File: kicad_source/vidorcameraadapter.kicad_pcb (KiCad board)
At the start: 2 copper layers, 62 x 47 mm, 44 parts, among them CN1 CONN_02X26, CN2 CONN_02X10, CN3 CONN_01X03

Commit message: added RGB led
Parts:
- removed W13, W14, W6, W7, W8: TEST_1P, wire_pads:SolderWirePad_single_1mmSMD
- added R19: 10k, resistors:R_0603, F.Cu at (147.3, 111.8)
- added R20: 10k, resistors:R_0603, F.Cu at (147.3, 114.5)
- added R21: 10k, resistors:R_0603, F.Cu at (151.0, 111.8)
- added R22: 10k, resistors:R_0603, F.Cu at (147.3, 117.1)
- added R23: 0R, resistors:R_0603, F.Cu at (90.0, 121.0)
- added R24: 0R, resistors:R_0603, F.Cu at (92.0, 121.0)
- added R25: 1k, resistors:R_0603, F.Cu at (156.0, 133.0)
- added R26: 1k, resistors:R_0603, F.Cu at (163.0, 126.0)
- added R27: 1k, resistors:R_0603, F.Cu at (171.0, 118.0)
- added R28: 1k, resistors:R_0603, F.Cu at (165.2, 131.0)
- added R29: 1k, resistors:R_0603, F.Cu at (169.0, 124.0)
- added R30: 1k, resistors:R_0603, F.Cu at (176.8, 118.0)
- added R31: 1k, resistors:R_0603, F.Cu at (172.0, 131.0)
- added R32: 1k, resistors:R_0603, F.Cu at (175.0, 125.0)
- R1, R10, R11, R12, R13, R14, R15, R16, R17, R18, R2, R3, R4, R5, R6, R7, R8, R9: value R_0603 -> 33R
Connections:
- CN1 pad 13: /RSVD9 -> /LED_R
- CN1 pad 14: /RSVD10 -> /SDA_V
- CN1 pad 16: /RSVD11 -> /SCL_V
- CN1 pad 17: /RSVD12 -> /LED_G
- CN1 pad 19: /RSVD13 -> /LED_B
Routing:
- net /SDA: track 3.49 -> 47.7 mm
- net /SCL: track 2.85 -> 47.0 mm
- net /SCL_V: track 0.00 -> 5.60 mm
- net /SDA_V: track 0.00 -> 5.06 mm
- net /RSVD11: track 3.63 -> 0.00 mm
- net /RSVD10: track 3.46 -> 0.00 mm
- net /RSVD9: track 2.33 -> 0.00 mm
- net /LED_R: track 0.00 -> 2.33 mm
- net /RSVD13: track 2.17 -> 0.00 mm
- net /LED_B: track 0.00 -> 2.17 mm
- net /RSVD12: track 2.08 -> 0.00 mm
- net /LED_G: track 0.00 -> 2.08 mm
- net +3V3: track 80.7 -> 82.0 mm

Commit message: placed all new parts in layout
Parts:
- added D1: Led_Small, LEDs:LED_0603, F.Cu at (79.7, 122.0)
- added D2: Led_Small, LEDs:LED_0603, F.Cu at (121.9, 127.3)
- added D3: Led_Small, LEDs:LED_0603, F.Cu at (125.3, 127.3)
- added D4: Led_Small, LEDs:LED_0603, F.Cu at (128.9, 92.4)
- added D5: Led_Small, LEDs:LED_0603, F.Cu at (117.7, 92.7)
- added D6: LED_RGB, LEDs:LED_RGB_PLLC-6, F.Cu at (124.8, 133.6)
- moved R25 76.7 mm to (79.7, 125.2), turned to 270 degrees
- moved R29 58.7 mm to (117.7, 95.5), turned to 270 degrees
- moved R30 58.1 mm to (120.4, 132.0), turned to 180 degrees
- moved R32 55.5 mm to (120.4, 135.2), turned to 180 degrees
- moved R31 51.7 mm to (120.4, 133.6), turned to 180 degrees
- moved R28 51.1 mm to (128.9, 95.2), turned to 270 degrees
- moved R27 46.2 mm to (125.3, 124.6), turned to 90 degrees
- moved R26 41.1 mm to (121.9, 124.6), turned to 90 degrees
- moved R21 34.9 mm to (119.3, 97.1), turned to 90 degrees
- moved R22 30.7 mm to (124.1, 97.1), turned to 90 degrees
- moved R20 25.1 mm to (132.3, 94.4), turned to 90 degrees
- moved R19 23.4 mm to (127.1, 100.0), turned to 90 degrees
- moved R10 0.10 mm to (120.9, 97.1)
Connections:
- R25 pad 1: (no net) -> Net-(D1-Pad2)
- R26 pad 1: (no net) -> Net-(D2-Pad2)
- R27 pad 1: (no net) -> Net-(D3-Pad2)
- R28 pad 1: (no net) -> Net-(D4-Pad2)
- R29 pad 1: (no net) -> Net-(D5-Pad2)
- R30 pad 1: (no net) -> Net-(D6-Pad1)
- R31 pad 1: (no net) -> Net-(D6-Pad2)
- R32 pad 1: (no net) -> Net-(D6-Pad3)
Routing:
- net +3V3: track 82.0 -> 142.5 mm, vias 3 -> 5
- net GND: track 162.2 -> 201.0 mm
- net /LED_R: track 2.33 -> 39.0 mm, vias 0 -> 2
- net /LED_G: track 2.08 -> 37.2 mm, vias 0 -> 2
- net /LED_B: track 2.17 -> 31.2 mm, vias 0 -> 2
- net /SCL: track 47.0 -> 54.5 mm
- net /PWDN_R: track 12.7 -> 17.8 mm
- net /HREF: track 32.4 -> 36.1 mm
- net Net-(D6-Pad3): track 0.00 -> 2.31 mm
- net Net-(D6-Pad1): track 0.00 -> 2.31 mm
- net /VSYNC: track 34.8 -> 36.9 mm
- net Net-(D6-Pad2): track 0.00 -> 2.10 mm
- net /XCLK: track 37.7 -> 36.0 mm
- net Net-(D1-Pad2): track 0.00 -> 1.65 mm
- net /SDA: track 47.7 -> 49.3 mm
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
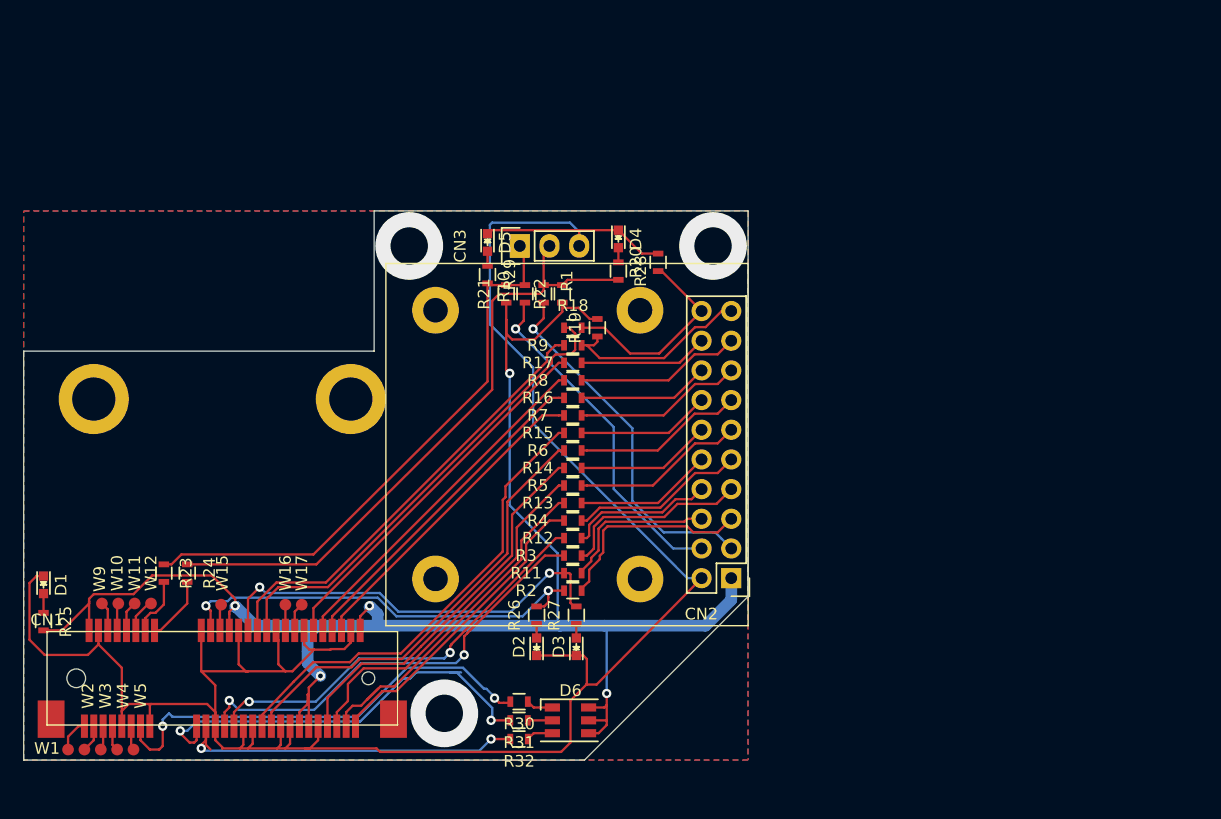
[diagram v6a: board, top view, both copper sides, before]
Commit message: moved camera connector to unblock HDMI connector on Vidor 4000, connected all traces again
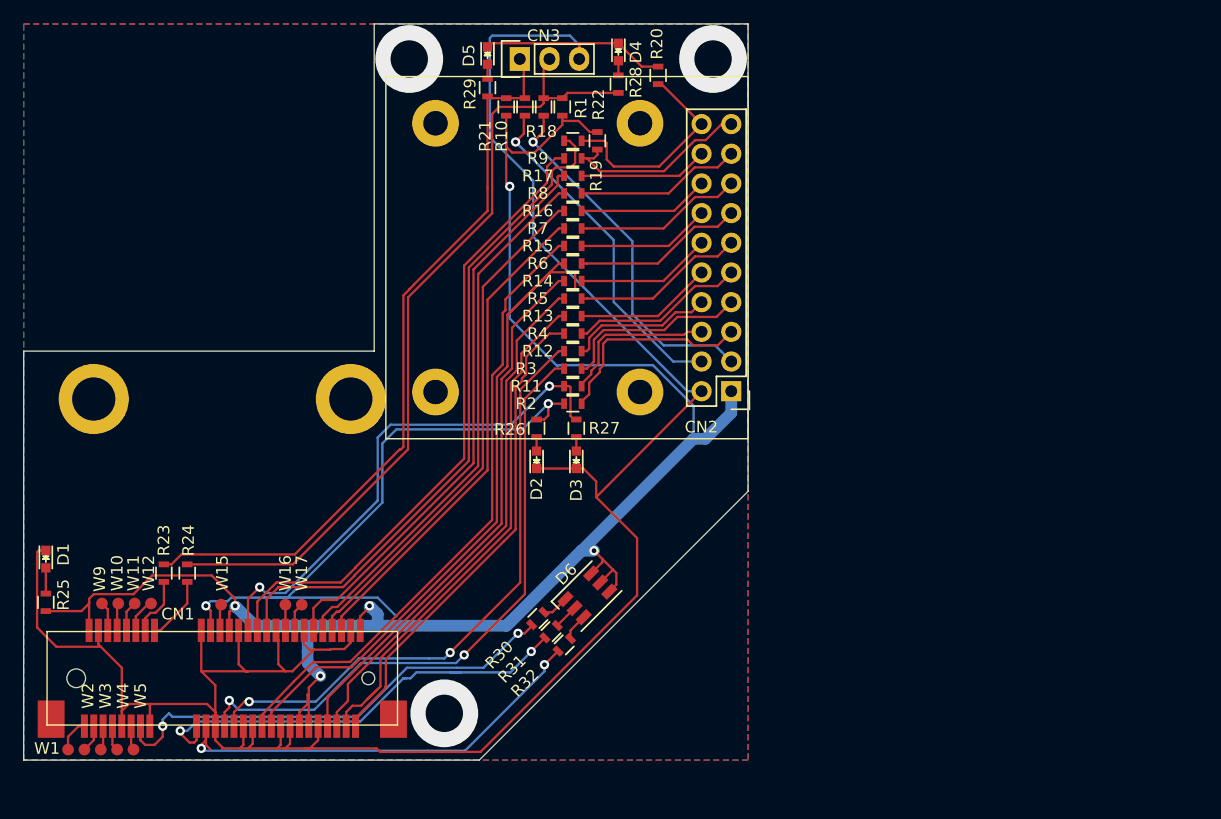
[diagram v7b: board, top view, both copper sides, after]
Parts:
- moved CN2 16.0 mm to (138.6, 105.4)
- moved CN3 16.0 mm to (120.5, 77.0)
- moved D2 16.0 mm to (121.9, 111.3)
- moved D3 16.0 mm to (125.3, 111.3)
- moved D4 16.0 mm to (128.9, 76.4)
- moved D5 16.0 mm to (117.7, 76.7)
- moved MECH3 16.0 mm to (113.2, 82.5)
- moved MECH4 16.0 mm to (113.2, 105.5)
- moved MECH5 16.0 mm to (130.8, 82.5)
- moved MECH6 16.0 mm to (130.8, 105.5)
- moved R1 16.0 mm to (122.5, 81.1)
- moved R10 16.0 mm to (120.9, 81.1)
- moved R11 16.0 mm to (125.0, 105.0)
- moved R12 16.0 mm to (125.0, 102.0)
- moved R13 16.0 mm to (125.0, 99.0)
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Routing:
- net /DOUT5: track 38.1 -> 60.7 mm
- net /VSYNC: track 36.9 -> 57.2 mm
- net +3V3: track 142.5 -> 162.2 mm
- net /DOUT0: track 32.0 -> 48.9 mm
- net /PWDN: track 40.7 -> 57.5 mm
- net /RST: track 38.2 -> 54.9 mm
- net /DOUT1: track 30.2 -> 46.5 mm
- net /XCLK: track 36.0 -> 51.9 mm
- net /DOUT2: track 28.8 -> 44.5 mm
- net /PCLK: track 37.7 -> 53.2 mm
- net /DOUT9: track 26.4 -> 41.7 mm
- net /DOUT8: track 29.6 -> 44.9 mm
- net /DOUT3: track 27.4 -> 42.6 mm
- net /SDA: track 49.3 -> 64.4 mm
- net GND: track 201.0 -> 216.0 mm
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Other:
- board size 62 x 47 mm -> 62 x 63 mm

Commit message: added logo and description on silkscreen
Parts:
- added G***: generationmake_logo, labels:generationmake_logo, B.Cu at (95.5, 132.5)
- added G***: LOGO, labels:107-systems_logo_big, B.Cu at (108.5, 112.4)
- added G***: LOGO, labels:107-systems_logo, F.Cu at (101.1, 112.4)
- moved D3 2.90 mm to (128.2, 111.3)
- moved R27 2.90 mm to (128.2, 108.6)
- moved D2 2.70 mm to (124.6, 111.3)
- moved R26 2.70 mm to (124.6, 108.6)
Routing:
- net /VSYNC: track 57.2 -> 41.7 mm
- net +3V3: track 162.2 -> 152.8 mm
- net /PWDN: track 57.5 -> 64.3 mm
- net /SCL: track 69.3 -> 74.7 mm
- net /DOUT2: track 44.5 -> 48.3 mm
- net /DOUT3: track 42.6 -> 46.3 mm
- net /RST: track 54.9 -> 58.7 mm
- net /DOUT0: track 48.9 -> 52.6 mm
- net /DOUT1: track 46.5 -> 50.2 mm
- net /SDA: track 64.4 -> 67.3 mm
- net /LED_B: track 38.7 -> 36.1 mm
- net /DOUT5: track 60.7 -> 58.4 mm
- net /LED_G: track 39.5 -> 37.7 mm
- net /DOUT4: track 53.9 -> 55.3 mm
- net /DOUT6: track 46.8 -> 48.1 mm
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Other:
- board text added: "Arducam OV2640 with M12 lens"
- board text added: "HREF"
- board text added: "PWR"
- board text added: "SCL"
- board text added: "SDA"
- board text added: "VSYNC"
- board text added: "VidorCameraAdapter 0.1"
- board text added: "bot"
- board text added: "see https://github.com/107-systems/VidorCameraAdapter for more information and documentation"
- board text added: "top"
- board text added: "use with Arduino MKR Vidor 4000"
